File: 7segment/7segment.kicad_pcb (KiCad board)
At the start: 2 copper layers, 101 parts, among them J1 Conn_01x05_Male, U1 74HC595, U2 74HC595, U3 74HC595, U4 74HC595

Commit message: tweaks
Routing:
- net Net-(D51-Pad2): track 63.4 -> 62.4 mm
- net Net-(D29-Pad2): track 63.0 -> 62.4 mm

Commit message: tweaks
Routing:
- net GND: track 18.7 -> 25.6 mm, vias 3 -> 4
- net Net-(D27-Pad2): track 29.4 -> 31.5 mm
- net Net-(D57-Pad2): track 29.5 -> 31.5 mm
- net Net-(D29-Pad2): track 62.4 -> 63.3 mm
- net Net-(D59-Pad2): track 62.3 -> 63.2 mm
- net Net-(D49-Pad2): track 30.5 -> 31.3 mm
- net Net-(D51-Pad2): track 62.4 -> 63.1 mm
- net Net-(D21-Pad2): track 61.0 -> 61.7 mm

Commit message: added label
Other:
- board text added: "Dat Clk SS +5V GND"
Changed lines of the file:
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@@
   (general
     (thickness 1.6)
-    (drawings 0)
+    (drawings 1)
     (tracks 482)
     (zones 0)
@@
     )
   )
+  (gr_text "Dat Clk  SS +5V GND" (at 85.344 118.872) (layer F.SilkS)
+    (effects (font (size 0.8 0.8) (thickness 0.1)))
+  )
   (segment (start 90.17 115.57) (end 90.17 116.84) (width 1) (layer F.Cu) (net 1))

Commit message: PCBway-compatibility
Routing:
- net GND: track 25.6 -> 0.00 mm, vias 4 -> 0
- net CLK: track 146.0 -> 126.1 mm
- net +5V: track 142.5 -> 130.2 mm
- net SS: track 92.4 -> 95.4 mm
- net D4: track 41.2 -> 40.1 mm

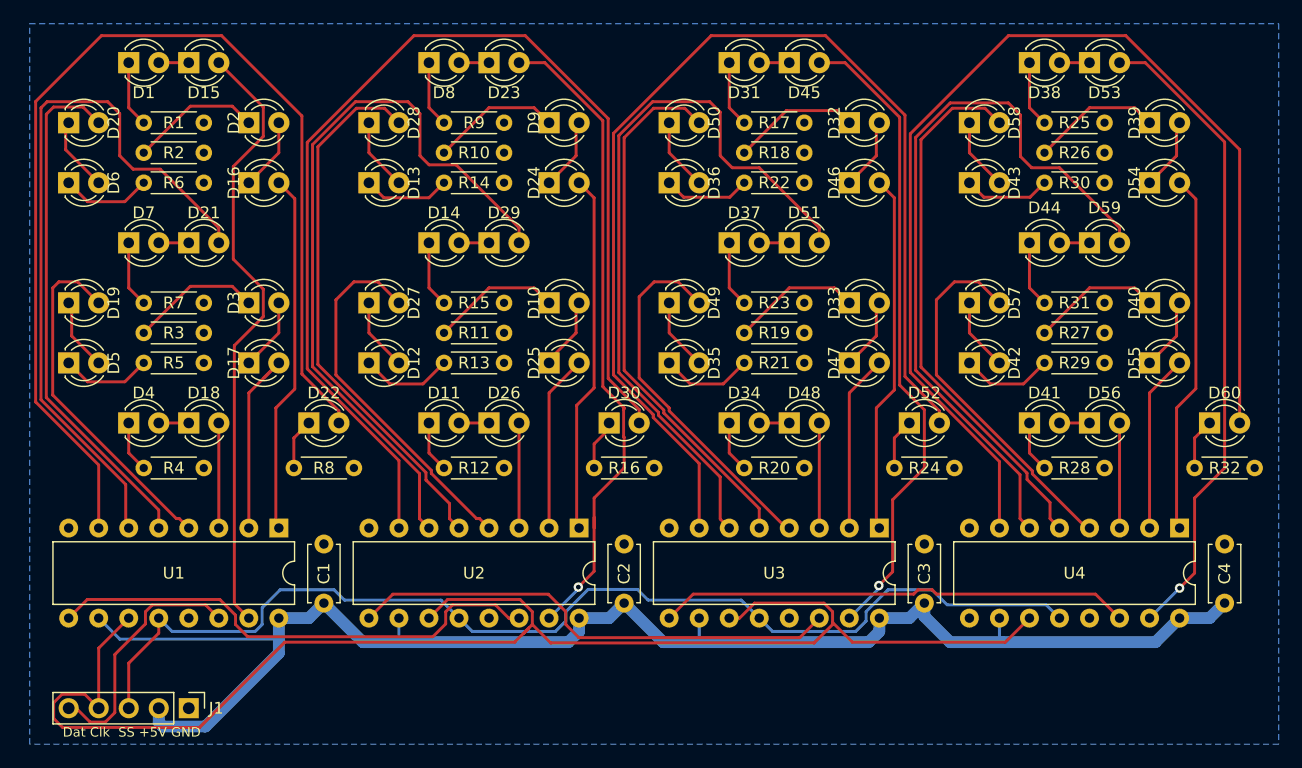
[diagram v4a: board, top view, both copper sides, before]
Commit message: resized to <100mm
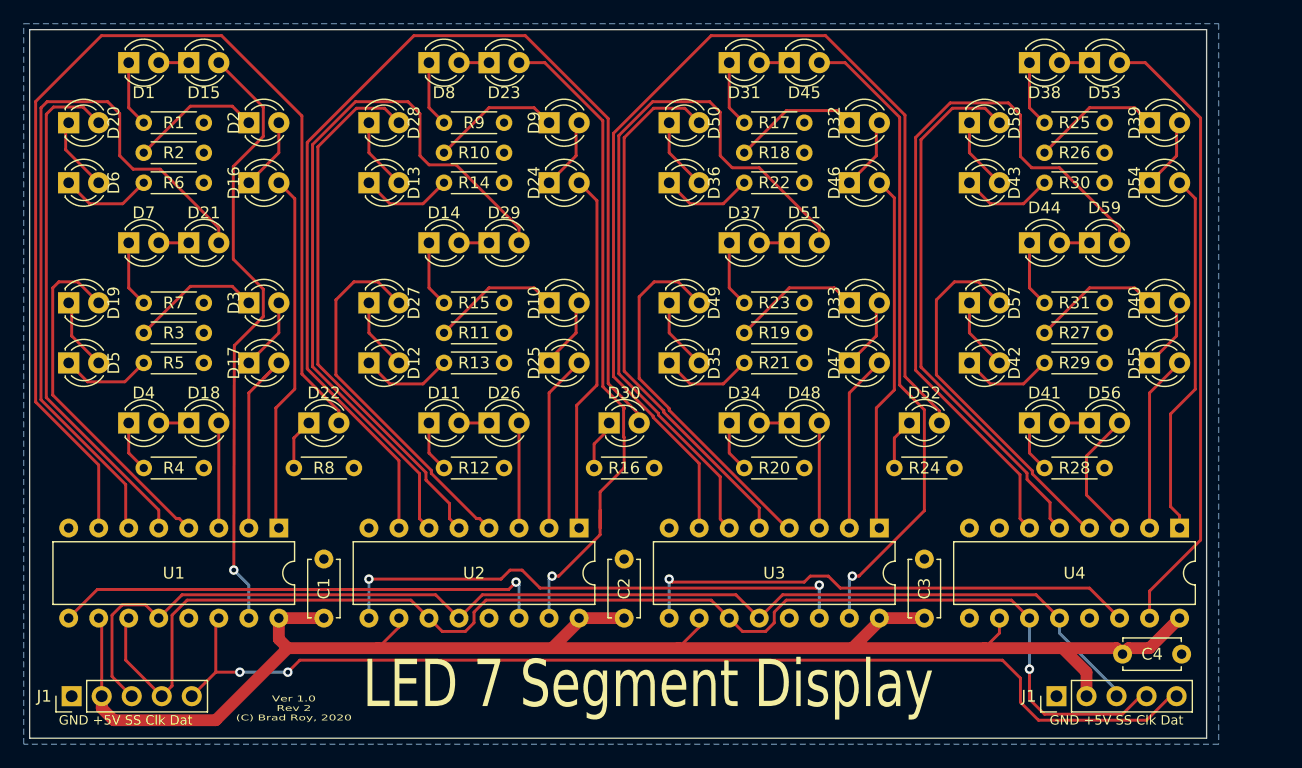
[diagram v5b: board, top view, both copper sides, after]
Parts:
- removed D60: LED, LED_THT:LED_D3.0mm
- removed R32: 2k7, Resistor_THT:R_Axial_DIN0204_L3.6mm_D1.6mm_P5.08mm_Horizontal
- added J1: Conn_01x05_Male, Connector_PinHeader_2.54mm:PinHeader_1x05_P2.54mm_Vertical, F.Cu at (163.6, 115.8)
- moved J1 9.96 mm to (80.3, 115.8), turned to 90 degrees
- moved C4 9.66 mm to (169.2, 112.3), turned to 0 degrees
- moved C1 1.27 mm to (101.6, 109.2)
- moved C2 1.27 mm to (127.0, 109.2)
- moved C3 1.27 mm to (152.4, 109.2)
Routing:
- net Net-(U4-Pad7): track 94.9 -> 0.00 mm
- net MOSI: track 21.2 -> 93.6 mm, vias 0 -> 2
- net CLK: track 126.1 -> 112.5 mm, vias 0 -> 1
- net +5V: track 130.2 -> 138.6 mm
- net SS: track 95.4 -> 101.5 mm
- net Net-(D60-Pad1): track 4.34 -> 0.00 mm
- net D3: track 41.8 -> 45.2 mm, vias 0 -> 2
- net D4: track 40.1 -> 43.2 mm, vias 0 -> 1
- net Net-(D56-Pad2): track 8.89 -> 11.2 mm
- net Net-(D53-Pad2): track 54.6 -> 52.9 mm, vias 1 -> 0
- net Net-(D23-Pad2): track 55.5 -> 56.5 mm
- net D2: track 42.7 -> 42.3 mm, vias 0 -> 1
- net Net-(D15-Pad2): vias 0 -> 1
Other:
- board outline added: 99.6 x 59.9 mm
- board text added: "GND +5V SS Clk Dat"
- board text added: "LED 7 Segment Display"
- board text added: "Ver 1.0 Rev 2 (C) Brad Roy, 2020"
- board text removed: "Dat Clk SS +5V GND"

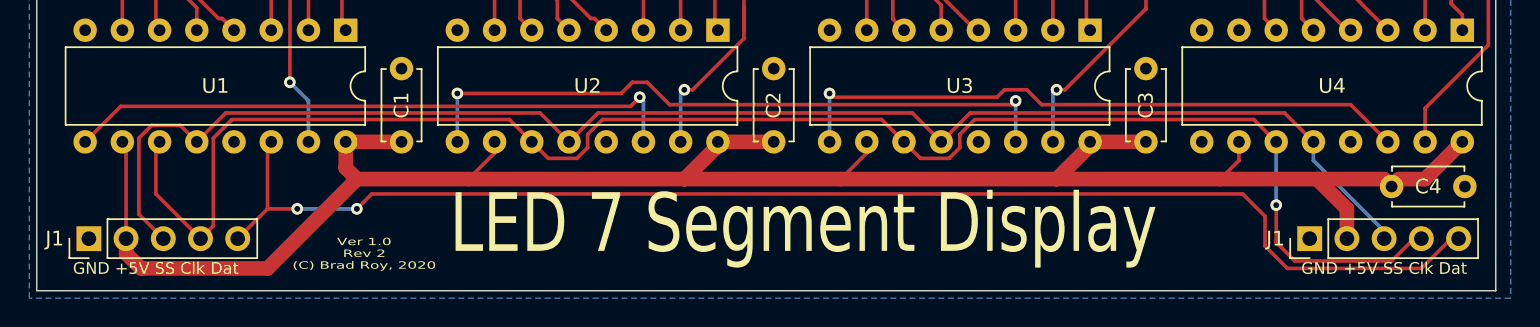
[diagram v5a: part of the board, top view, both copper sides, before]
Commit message: Added daisy-chain connector
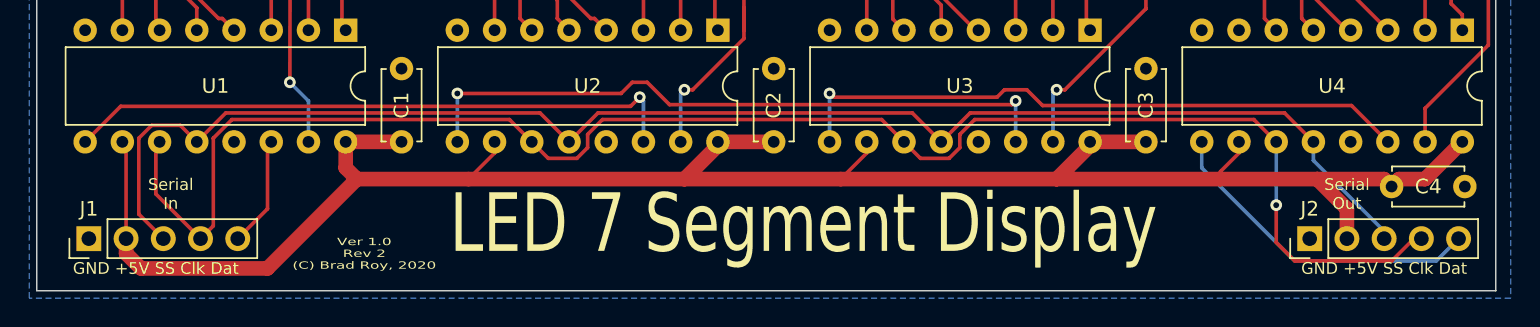
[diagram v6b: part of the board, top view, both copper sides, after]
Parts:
- removed the J1 at (163.6, 115.8)
- added J2: Conn_01x05_Male, Connector_PinHeader_2.54mm:PinHeader_1x05_P2.54mm_Vertical, F.Cu at (163.6, 115.8)
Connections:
- U4 pad 9: Net-(U4-Pad9) -> OUT
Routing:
- net MOSI: track 93.6 -> 7.55 mm, vias 2 -> 0
- net OUT: track 0.00 -> 22.6 mm
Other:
- board text added: "Serial In"
- board text added: "Serial Out"
